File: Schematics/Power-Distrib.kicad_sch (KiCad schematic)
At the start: 62 parts, among them J63 Screw_Terminal_01x02, J64 Screw_Terminal_01x02, J65 Screw_Terminal_01x02, J66 Conn_01x03, J67 Conn_01x03, J68 Conn_01x03, J69 Conn_01x03, J70 Conn_01x02, J71 Conn_01x02, J72 Conn_01x02, J73 Conn_01x02, J74 Conn_01x02, J75 Conn_01x02, J76 Conn_01x02, J77 Conn_01x02, J78 Conn_01x03, J79 Conn_01x03, J80 Conn_01x03, J81 Conn_01x03, J82 Conn_01x03, J83 Conn_01x03, J84 Conn_01x02, J85 Jack-DC, J86 Jack-DC, J87 Conn_01x03, J88 Conn_01x03, K1 Relay_SPDT, U87 LM7805, U88 LM7812, U89 LM7912, U90 LM7805, U91 LM7812, U92 LM7912

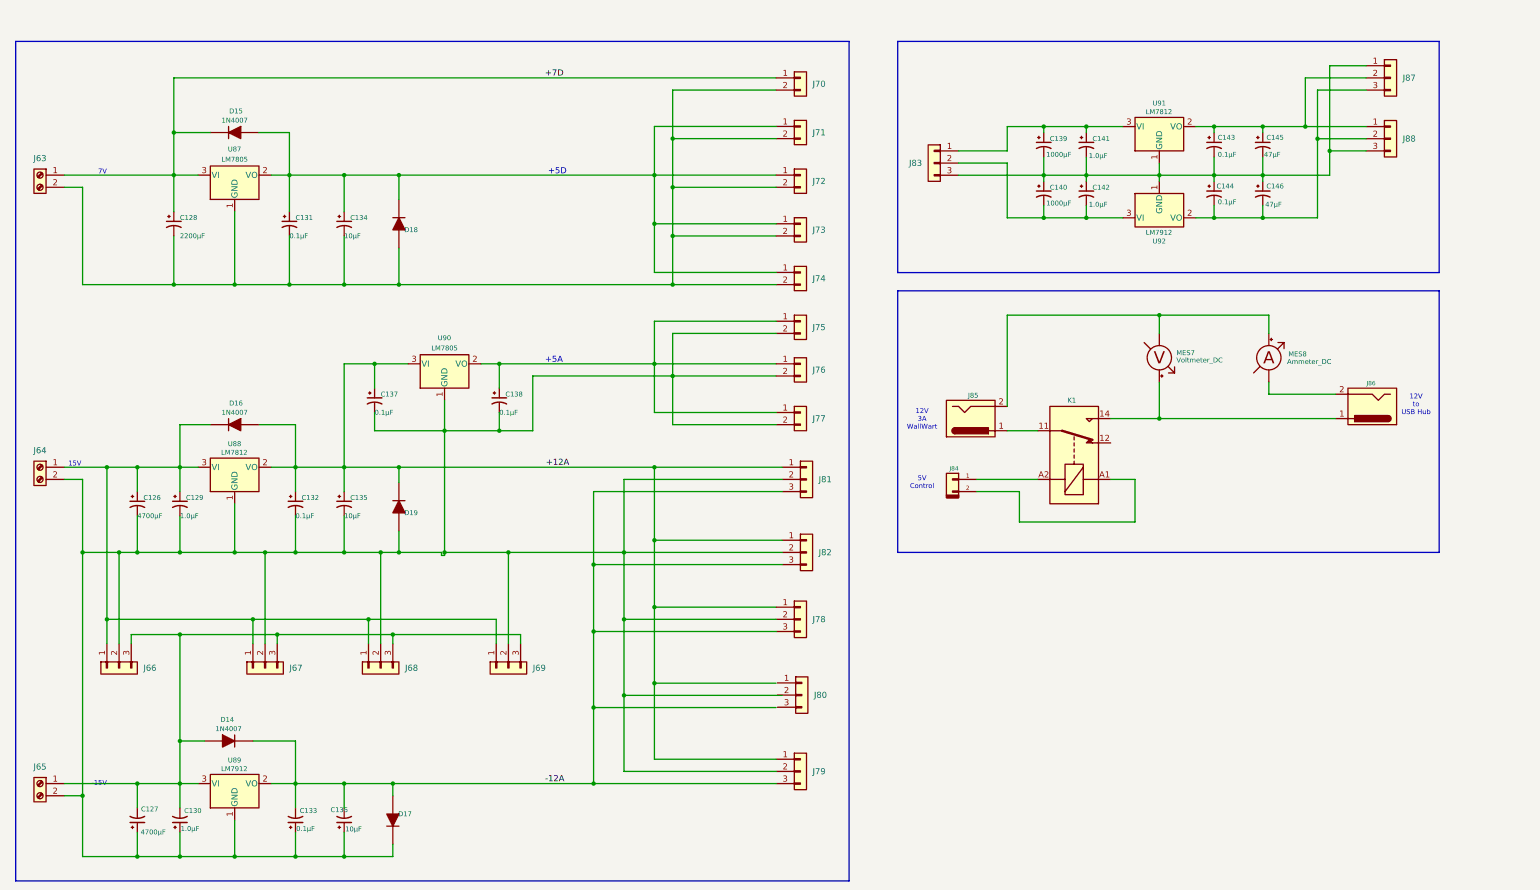
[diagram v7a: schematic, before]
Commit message: Adding in partion LFO-2.  Changed keboard buttons to momentary and encoders to just direction.
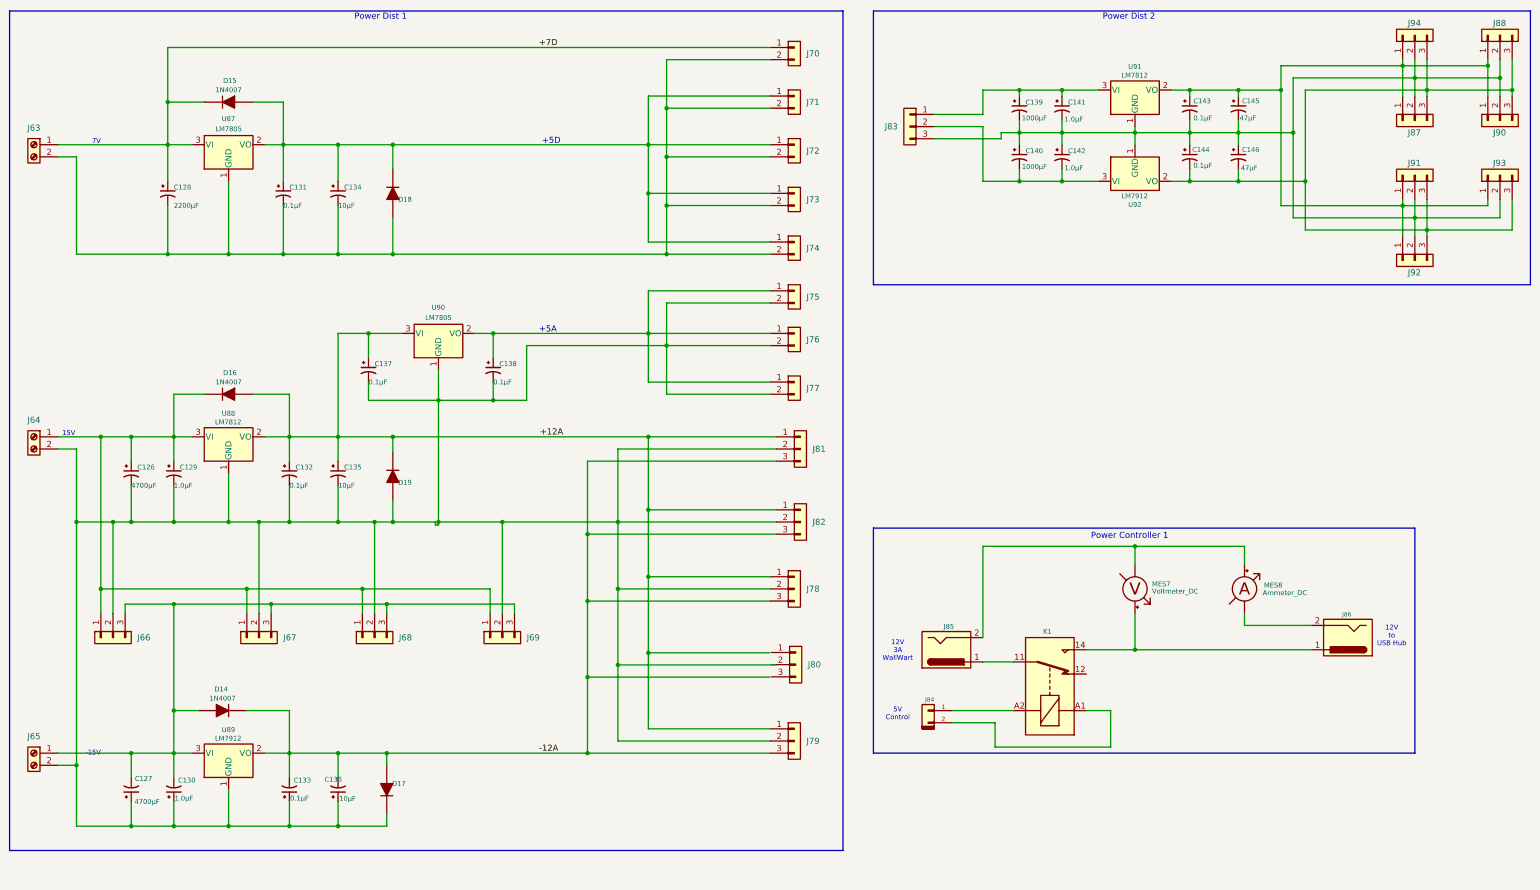
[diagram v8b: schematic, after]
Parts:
- added J90, J91, J92, J93, J94: Conn_01x03, symbol Connector_Generic:Conn_01x03
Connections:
- net at C139.2, C140.1, C141.2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: now also J87.2 (Pin_2), J88.2 (Pin_2), J90.2 (Pin_2), J91.2 (Pin_2), J92.2 (Pin_2), J93.2 (Pin_2), J94.2 (Pin_2); no longer J87.1 (Pin_1), J88.3 (Pin_3)
- net at C143.1, C145.1, J88.1 (Pin_1)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: now also J87.1 (Pin_1), J90.1 (Pin_1), J91.1 (Pin_1), J92.1 (Pin_1), J93.1 (Pin_1), J94.1 (Pin_1); no longer J87.2 (Pin_2)
- net at C144.2, C146.2, J87.3 (Pin_3)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: now also J88.3 (Pin_3), J90.3 (Pin_3), J91.3 (Pin_3), J92.3 (Pin_3), J93.3 (Pin_3), J94.3 (Pin_3); no longer J88.2 (Pin_2)
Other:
- note added: "Power Controller 1"
- note added: "Power Dist 1"
- note added: "Power Dist 2"
- moved on the sheet: C126, C127, C128, C129, C130, C131, C132, C133, C134, C135, C136, C137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
